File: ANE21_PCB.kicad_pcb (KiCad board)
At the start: 4 copper layers, 74.6 x 66 mm, 60 parts, among them J13 1-2199119-5, J15 USB_OTG, J16 Conn_01x02, J2 Barrel_Jack, J3 USB-A-S-VT, J5 690-019-298-412, J6 Conn_02x07_Odd_Even, J7 2036150003 (USB-C_Connector), U1 74LVC1G07SE-7, U10 PUSB3FR4, U11 TPD4EUSB30, U12 SI-51005-F, U13 RT9742SNGV, U2 74LVC1G07SE-7, U3 HUSB238_xxxDD, U4 AP62300WU-7, U8 AP62300WU-7, U9 PUSB3FR4

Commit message: Small changes to routes
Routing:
- net /+3.3v: track 177.2 -> 220.4 mm
- net /CM4_LowSpeed/TRD1_P: track 70.1 -> 73.1 mm
- net /CM4_LowSpeed/TRD3_N: track 60.8 -> 62.4 mm
- net /CM4_LowSpeed/TRD2_P: track 67.4 -> 68.9 mm
- net /CM4_LowSpeed/TRD0_P: track 62.8 -> 63.9 mm
- net /CM4_LowSpeed/TRD1_N: track 72.6 -> 73.7 mm
- net /CM4_LowSpeed/TRD2_N: track 67.0 -> 67.9 mm

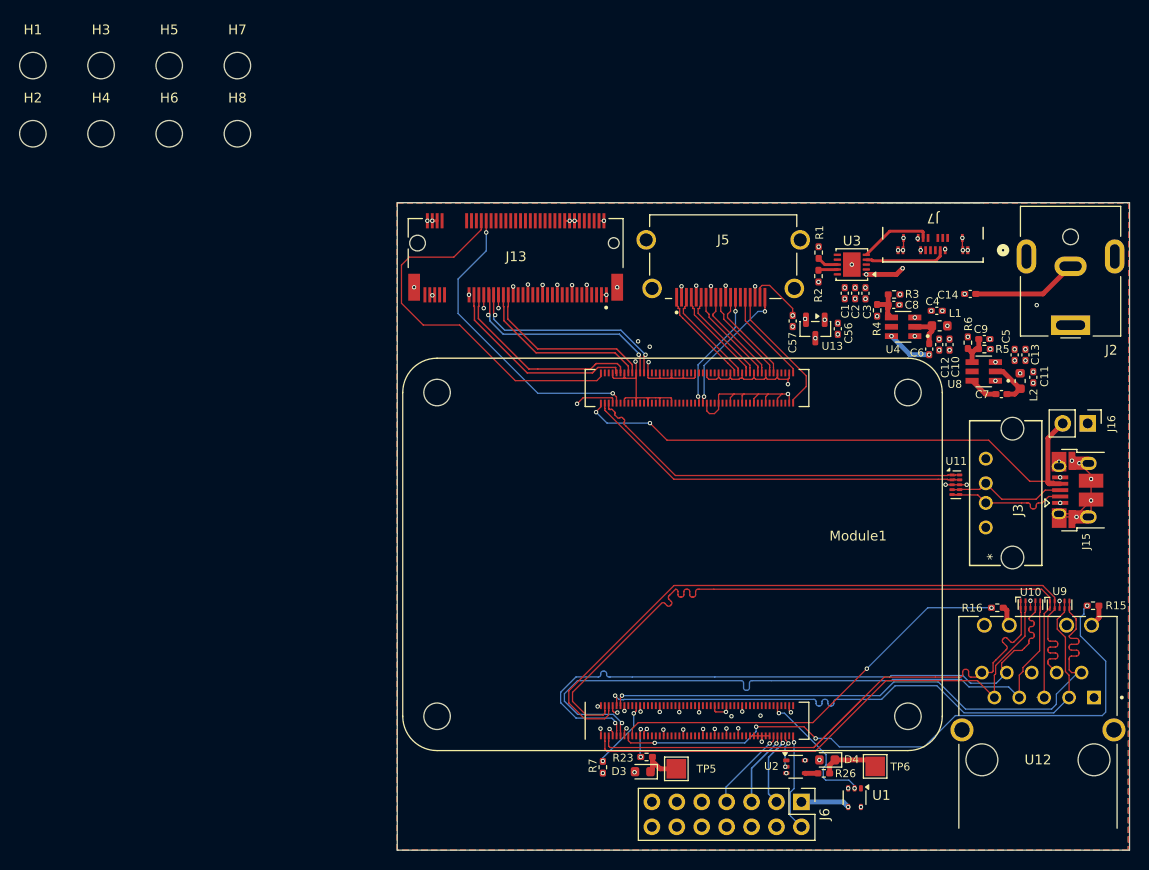
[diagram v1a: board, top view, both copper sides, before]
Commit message: Redid traces with correct requirements, needs double checking.
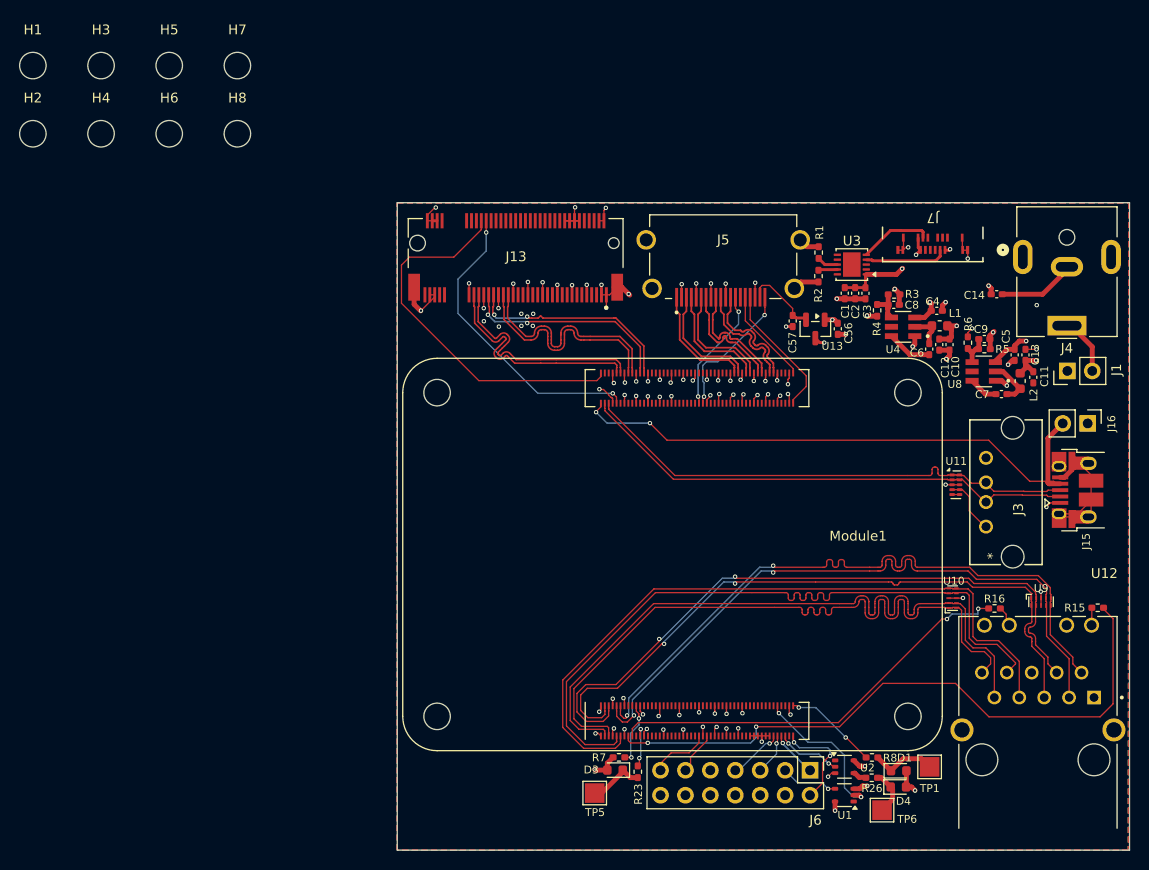
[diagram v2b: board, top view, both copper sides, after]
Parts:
- removed J2: Barrel_Jack, Connector_BarrelJack:BarrelJack_CUI_PJ-063AH_Horizontal
- added D1: LED Green, LED_SMD:LED_0603_1608Metric, F.Cu at (111.8, 106.9)
- added J1: Conn_01x02, Connector_PinHeader_2.54mm:PinHeader_1x02_P2.54mm_Vertical, F.Cu at (129.0, 66.2)
- added J4: Barrel_Jack, Connector_BarrelJack:BarrelJack_CUI_PJ-063AH_Horizontal, F.Cu at (128.9, 61.5)
- added R8: 1k, Resistor_SMD:R_0402_1005Metric_Pad0.72x0.64mm_HandSolder, F.Cu at (109.1, 105.5)
- added TP1: TestPoint, TestPoint:TestPoint_Pad_2.0x2.0mm, F.Cu at (114.9, 106.5)
- U12: footprint SI-51005-F:BEL_SI-51005-F -> lib:BEL_SI-51005-F
- moved TP5 8.68 mm to (80.8, 109.2)
- moved U10 7.96 mm to (117.3, 89.3), turned to 90 degrees
- moved D4 7.77 mm to (111.8, 108.6), turned to 0 degrees
- moved U2 4.98 mm to (106.3, 106.5)
- moved R26 4.91 mm to (109.0, 107.6)
- moved TP6 4.51 mm to (110.1, 110.9)
- moved J6 3.34 mm to (102.8, 106.9)
- moved D3 2.83 mm to (82.9, 106.8)
- moved C14 2.70 mm to (121.8, 58.3)
- moved R7 1.93 mm to (83.3, 105.5), turned to 180 degrees
- moved U9 1.92 mm to (126.3, 89.7)
- moved R23 1.75 mm to (85.2, 107.0), turned to -90 degrees
- moved U1 1.07 mm to (106.2, 109.4), turned to 180 degrees
- moved R15 0.51 mm to (132.1, 90.3), turned to 180 degrees
- moved R16 0.29 mm to (121.6, 90.4)
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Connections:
- J15 pad 2: pUSBD- -> USBD-
- J15 pad 3: pUSBD+ -> USBD+
- J3 pad 2: pUSBD- -> USBD-
- J3 pad 3: pUSBD+ -> USBD+
- J6 pad 1: Net-(J6-Pin_1) -> /CM4_LowSpeed/nRPIBOOT
- J6 pad 11: unconnected-(J6-Pin_11-Pad11) -> /GPIO14
- J6 pad 13: /+5v -> /GPIO15
- J6 pad 3: /CM4_LowSpeed/nRPIBOOT -> /Miscellaneous/Reset
- Module1 pad 100: /nEXTRST -> Net-(Module1A-nEXTRST)
- Module1 pad 51: /CM4_LowSpeed/GPIO15 -> /GPIO15
- Module1 pad 55: /CM4_LowSpeed/GPIO14 -> /GPIO14
- U1 pad 4: Net-(J6-Pin_1) -> /Miscellaneous/Reset
- U11 pad 4: pUSBD+ -> /+5v
- U11 pad 5: pUSBD- -> Net-(U11-D2-)
- U11 pad 6: pUSBD- -> Net-(U11-D2-)
- U11 pad 7: pUSBD+ -> /+5v
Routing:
- net GND: track 188.3 -> 137.9 mm, vias 87 -> 96
- net /+3.3v: track 220.4 -> 266.5 mm, vias 14 -> 8
- net /CM4_LowSpeed/TRD3_P: track 56.4 -> 72.1 mm
- net pUSBD-: track 13.1 -> 0.00 mm
- net pUSBD+: track 12.6 -> 0.00 mm
- net /+5v: track 36.1 -> 24.3 mm, vias 10 -> 6
- net USBD+: track 39.8 -> 51.5 mm
- net USBD-: track 39.9 -> 51.6 mm
- net Net-(Module1A-nEXTRST): track 0.00 -> 9.75 mm, vias 0 -> 2
- net /CM4_LowSpeed/TRD3_N: track 62.4 -> 72.0 mm
- net /+12v: track 45.3 -> 52.3 mm, vias 12 -> 5
- net Net-(D1-K): track 0.00 -> 6.71 mm
- net /CM4_LowSpeed/TRD0_N: track 62.4 -> 68.9 mm, vias 1 -> 2
- net /GPIO15: track 0.00 -> 6.30 mm
- net /Miscellaneous/Reset: track 0.00 -> 5.88 mm, vias 0 -> 1
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- removed copper zone on B.Cu, net /CM4_HighSpeed/HDMI0_CK_N
- removed copper zone on F.Cu, net /CM4_HighSpeed/HDMI0_CK_N

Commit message: Very small changes made, dunno what
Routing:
- net /+5v: track 24.3 -> 20.1 mm
- net GND: track 137.9 -> 140.3 mm, vias 96 -> 129

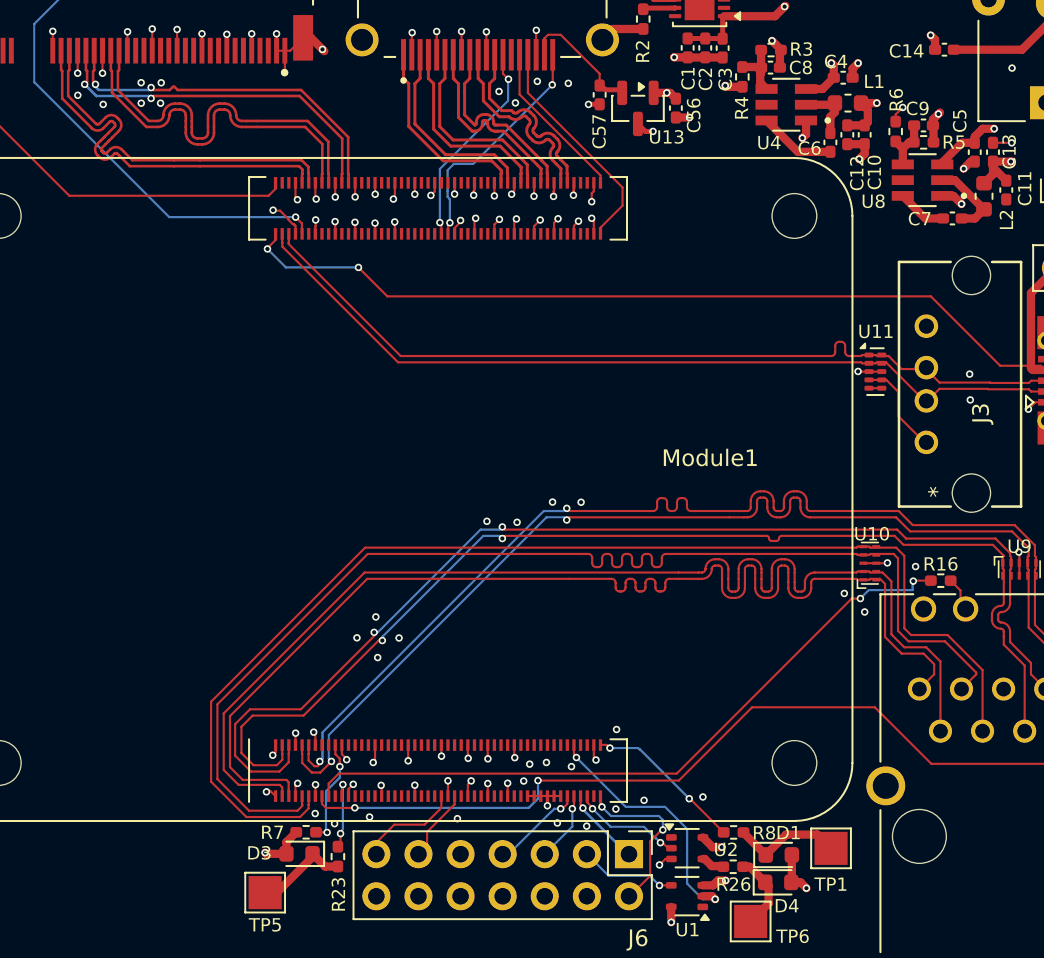
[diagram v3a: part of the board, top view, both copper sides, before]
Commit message: Adjusted 3.3v for CM4 3.3v output, PCIe stayed the same.
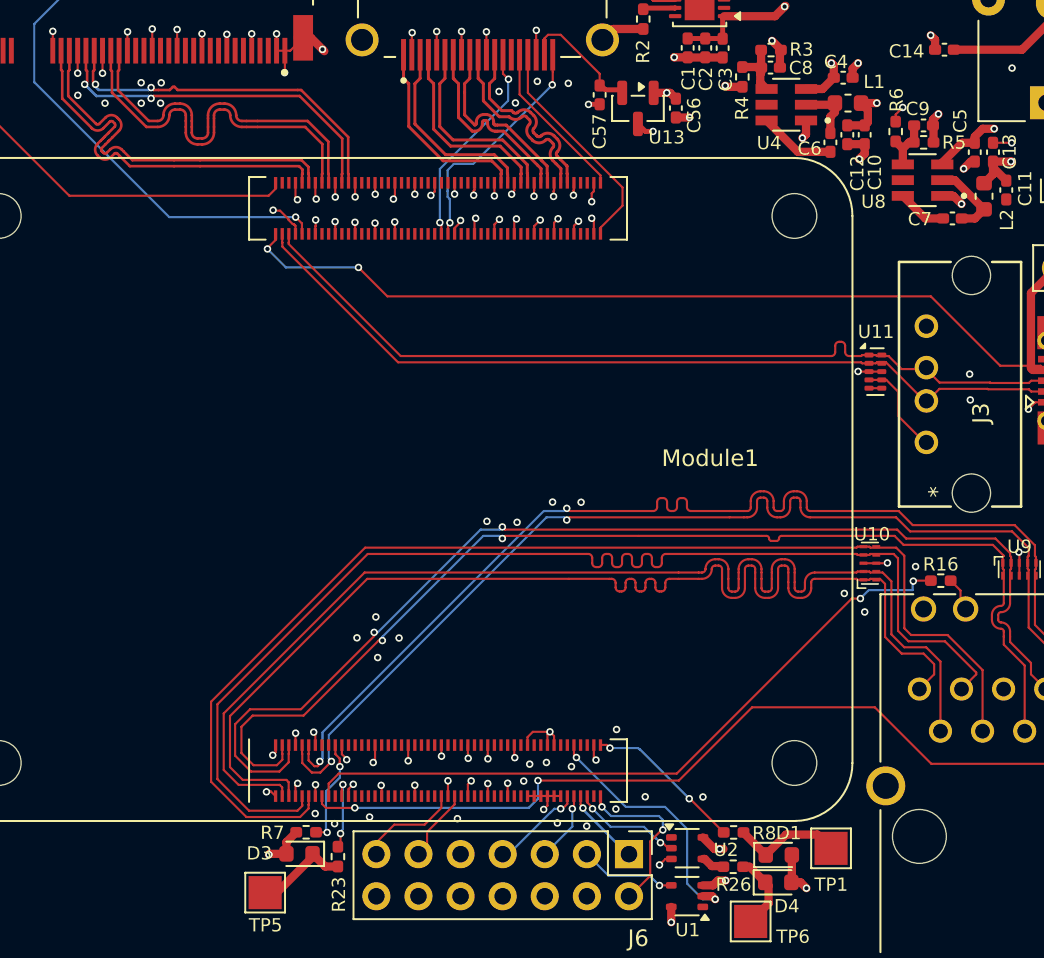
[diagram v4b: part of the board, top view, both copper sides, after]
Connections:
- D1 pad 2: /+3.3v -> /3.3V OUT (CM4.86)
- D3 pad 2: /+3.3v -> /3.3V OUT (CM4.86)
- D4 pad 2: /+3.3v -> /3.3V OUT (CM4.86)
- Module1 pad 78: unconnected-(Module1A-GPIO_VREF(1.8v/3.3v_Input)-Pad78) -> /3.3V OUT (CM4.86)
- Module1 pad 84: 3.3V OUT (CM4.84) -> /3.3V OUT (CM4.86)
- Module1 pad 86: 3.3V OUT (CM4.86) -> /3.3V OUT (CM4.86)
- Module1 pad 88: 1.8V OUT (CM4.88) -> unconnected-(Module1A-+1.8v_(Output)-Pad88)
- Module1 pad 90: 1.8V OUT (CM4.90) -> unconnected-(Module1A-+1.8v_(Output)-Pad90)
- R7 pad 2: /+3.3v -> /3.3V OUT (CM4.86)
- U12 pad 14: /+3.3v -> /3.3V OUT (CM4.86)
- U12 pad 16: /+3.3v -> /3.3V OUT (CM4.86)
- U2 pad 5: /+3.3v -> /3.3V OUT (CM4.86)
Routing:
- net /+3.3v: track 266.5 -> 122.8 mm, vias 8 -> 5
- net /3.3V OUT (CM4.86): track 0.00 -> 96.3 mm, vias 0 -> 4
- net /+5v: track 20.1 -> 77.8 mm
- added copper zone on In2.Cu, net GND
- removed copper zone on In2.Cu, net /+5v

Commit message: Hehe, smol board now
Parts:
- removed C14: 100nF, Capacitor_SMD:C_0402_1005Metric_Pad0.74x0.62mm_HandSolder
- removed J15: USB_OTG, Connector_USB:USB_Micro-B_Amphenol_10103594-0001LF_Horizontal
- removed J16: Conn_01x02, Connector_PinHeader_2.54mm:PinHeader_1x02_P2.54mm_Vertical
- removed J4: Barrel_Jack, Connector_BarrelJack:BarrelJack_CUI_PJ-063AH_Horizontal
- added J2: 2036150003 (USB-C_Connector), USB-C:CONN_2036150003_MOL(USB-c_connector), B.Cu at (118.4, 78.8)
- C1, C10, C11, C12, C13, C2, C3, C4, C5, C6, C7, C8, C9, J1, J3, J7, L1, L2, R1, R15, R16, R2, R3, R4, R5, R6, U12, U3, U4, U8: moved to B.Cu
- moved U12 54.8 mm to (77.0, 81.3)
- moved R15 48.3 mm to (84.3, 97.0)
- moved R16 48.1 mm to (73.9, 97.0), turned to 0 degrees
- moved U9 46.9 mm to (80.1, 97.9), turned to 90 degrees
- moved U10 41.7 mm to (77.4, 101.6)
- moved J7 40.0 mm to (118.2, 90.4), turned to -90 degrees
- moved R1 39.5 mm to (108.6, 93.3), turned to -90 degrees
- moved C13 37.4 mm to (99.1, 91.8)
- moved U3 37.1 mm to (111.3, 92.2)
- moved C11 35.6 mm to (100.1, 91.8), turned to -90 degrees
- moved R6 35.0 mm to (105.8, 95.8), turned to 180 degrees
- moved R2 34.8 mm to (108.6, 90.9), turned to 90 degrees
- moved R5 34.2 mm to (105.8, 94.8), turned to 0 degrees
- moved C9 34.2 mm to (105.8, 93.8), turned to 180 degrees
- moved L2 33.2 mm to (101.4, 91.4), turned to -90 degrees
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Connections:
- R7 pad 1: Net-(Module1A-EEPROM_nWP) -> /3.3V OUT (CM4.86)
- R7 pad 2: /3.3V OUT (CM4.86) -> Net-(Module1A-EEPROM_nWP)
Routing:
- net USB_OTG: track 59.4 -> 0.00 mm, vias 2 -> 0
- net /CM4_LowSpeed/LEDG: track 65.3 -> 6.61 mm, vias 2 -> 1
- net /CM4_LowSpeed/TRD2_P: track 72.3 -> 23.3 mm
- net /CM4_LowSpeed/TRD2_N: track 72.2 -> 23.3 mm
- net /CM4_LowSpeed/TRD3_P: track 72.1 -> 23.3 mm
- net /CM4_LowSpeed/TRD3_N: track 72.0 -> 23.3 mm
- net /CM4_LowSpeed/TRD1_N: track 69.1 -> 23.1 mm, vias 2 -> 0
- net /CM4_LowSpeed/TRD1_P: track 69.2 -> 23.2 mm, vias 2 -> 0
- net /CM4_LowSpeed/TRD0_N: track 68.9 -> 23.2 mm, vias 2 -> 0
- net /CM4_LowSpeed/TRD0_P: track 68.8 -> 23.2 mm, vias 2 -> 0
- net /+5v: track 77.8 -> 122.4 mm, vias 6 -> 10
- net /CM4_LowSpeed/LEDY: track 42.5 -> 13.7 mm, vias 2 -> 1
- net /+3.3v: track 122.8 -> 95.3 mm, vias 5 -> 2
- net /+12v: track 52.3 -> 25.2 mm, vias 5 -> 0
- net GND: track 140.3 -> 125.7 mm, vias 129 -> 110
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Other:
- board size 74.6 x 66 mm -> 59.3 x 63.9 mm
